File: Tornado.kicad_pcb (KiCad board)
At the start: 4 copper layers, 22.9 x 22.9 mm, 42 parts, among them J1 MOLEX, SW1 ID, U1 AP63205WU, U2 STM32G431KBUx, U3 LSM6DS3, U4 AP2112K-3.3, U5 TCAN1057A, Y1 32MHz

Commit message: Fixed silkscreen
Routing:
- net /ID_SW: track 16.1 -> 17.7 mm
- net /SDA: track 27.1 -> 26.5 mm

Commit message: Changed ESD diode
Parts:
- D2: value ~ -> TVS; footprint Tornado_Footprints:TVS-2020 -> Diode_SMD:D_SOD-323
- U3: value LSM6DS3 -> LSM6DSV
- moved D2 0.10 mm to (148.5, 106.6)
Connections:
- D2 pad 1: GND -> +12V
- D2 pad 2: +12V -> GND
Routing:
- net GND: track 87.8 -> 81.9 mm, vias 19 -> 20

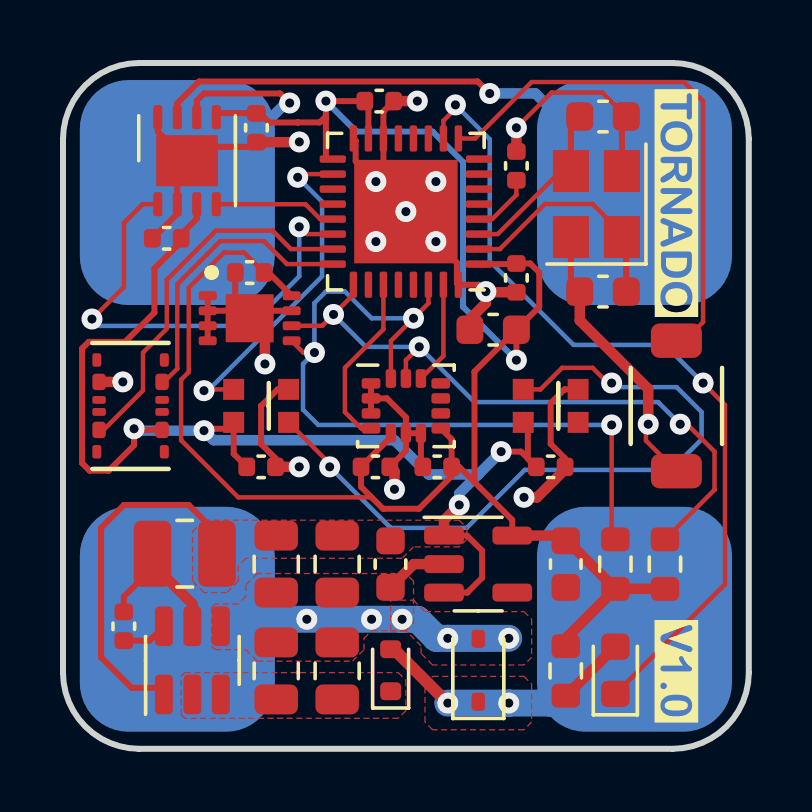
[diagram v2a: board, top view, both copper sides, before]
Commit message: Replaced pads with holes
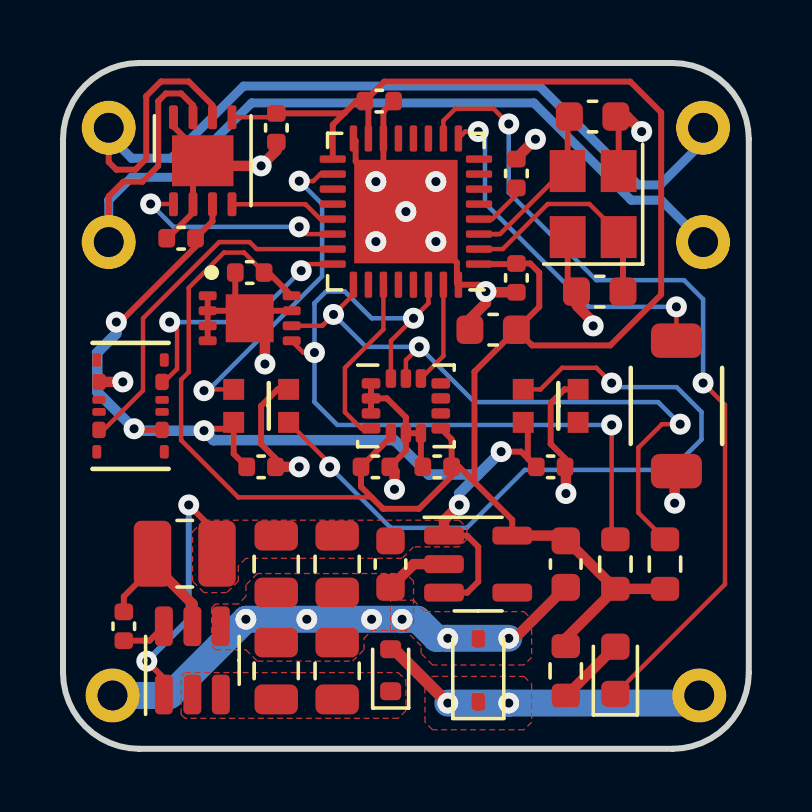
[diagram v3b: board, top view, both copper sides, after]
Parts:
- removed TP1: PWR, Tornado_Footprints:Wire_Pad
- removed TP2: GND, Tornado_Footprints:Wire_Pad
- removed TP3: CANH, Tornado_Footprints:Wire_Pad
- removed TP4: CANL, Tornado_Footprints:Wire_Pad
- added J2: PWR, Tornado_Footprints:Wire_Hole, F.Cu at (155.8, 107.4)
- added J3: CANH, Tornado_Footprints:Wire_Hole, F.Cu at (156.0, 92.3)
- added J3: CANH, Tornado_Footprints:Wire_Hole, F.Cu at (136.1, 92.3)
- added J4: CANL, Tornado_Footprints:Wire_Hole, F.Cu at (156.0, 88.5)
- added J4: CANL, Tornado_Footprints:Wire_Hole, F.Cu at (136.1, 88.5)
- added J5: GND, Tornado_Footprints:Wire_Hole, F.Cu at (136.3, 107.4)
- moved C10 0.66 mm to (141.7, 88.5)
- moved U5 0.52 mm to (139.3, 89.6)
- moved C9 0.48 mm to (138.6, 92.2)
- moved C15 0.35 mm to (152.3, 88.1)
- moved C20 0.25 mm to (149.7, 90.0)
- moved C16 0.11 mm to (152.5, 94.0)
- moved Y1 0.11 mm to (152.3, 91.1)
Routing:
- net /CANL: track 8.86 -> 31.7 mm, vias 1 -> 0
- net /CANH: track 17.5 -> 32.1 mm, vias 1 -> 0
- net /TX: track 15.6 -> 7.25 mm
- net +3.3V: track 68.7 -> 76.2 mm, vias 2 -> 0
- net +5V: track 52.3 -> 44.9 mm, vias 4 -> 7
- net /ID_SW: track 17.7 -> 12.4 mm, vias 0 -> 2
- net GND: track 81.9 -> 78.2 mm, vias 20 -> 22
- net +12V: track 10.0 -> 11.1 mm
- net /SWCLK: track 9.60 -> 8.58 mm, vias 0 -> 2
- net /SDA: track 26.5 -> 25.9 mm
- net /SWDIO: track 12.5 -> 11.9 mm
- net /RX: track 4.14 -> 3.56 mm

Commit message: Added Silkscreen
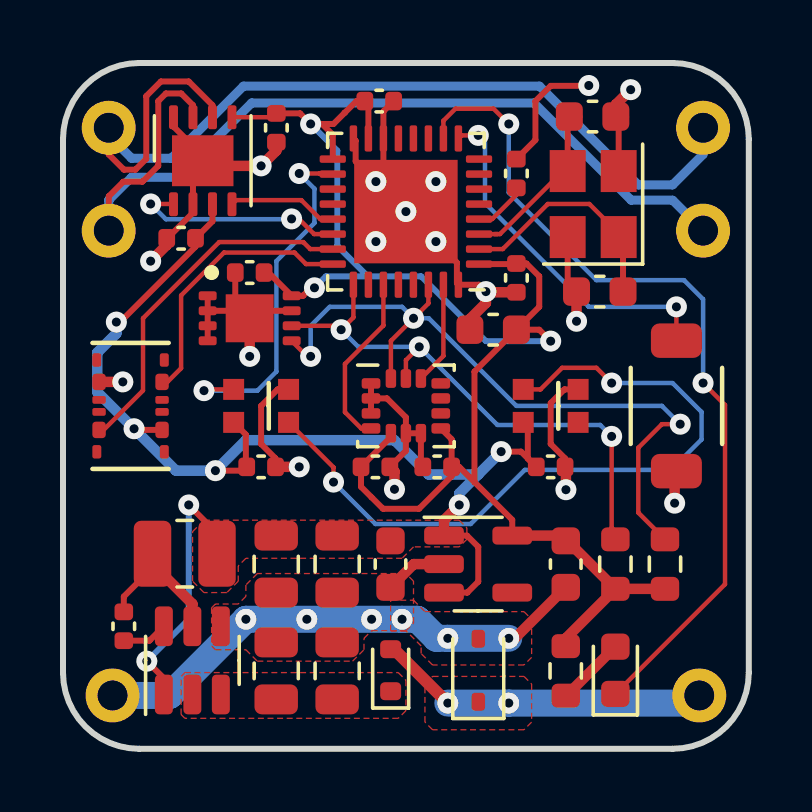
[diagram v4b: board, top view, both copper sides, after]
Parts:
- moved R1 1.65 mm to (153.0, 103.1)
- moved R2 1.65 mm to (154.7, 103.1)
- moved J3 0.38 mm to (156.0, 91.9)
- moved J3 0.38 mm to (136.1, 91.9)
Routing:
- net +3.3V: track 76.2 -> 55.4 mm, vias 0 -> 3
- net /SCL: track 22.4 -> 18.7 mm
- net GND: track 78.2 -> 81.5 mm, vias 22 -> 23
- net +5V: track 44.9 -> 46.0 mm
- net /RGB: track 11.2 -> 12.2 mm
- net /CANH: track 32.1 -> 31.1 mm
- net /SDA: track 25.9 -> 25.0 mm
- net /SWCLK: track 8.58 -> 9.06 mm, vias 2 -> 0

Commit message: Added Ferrite Bead
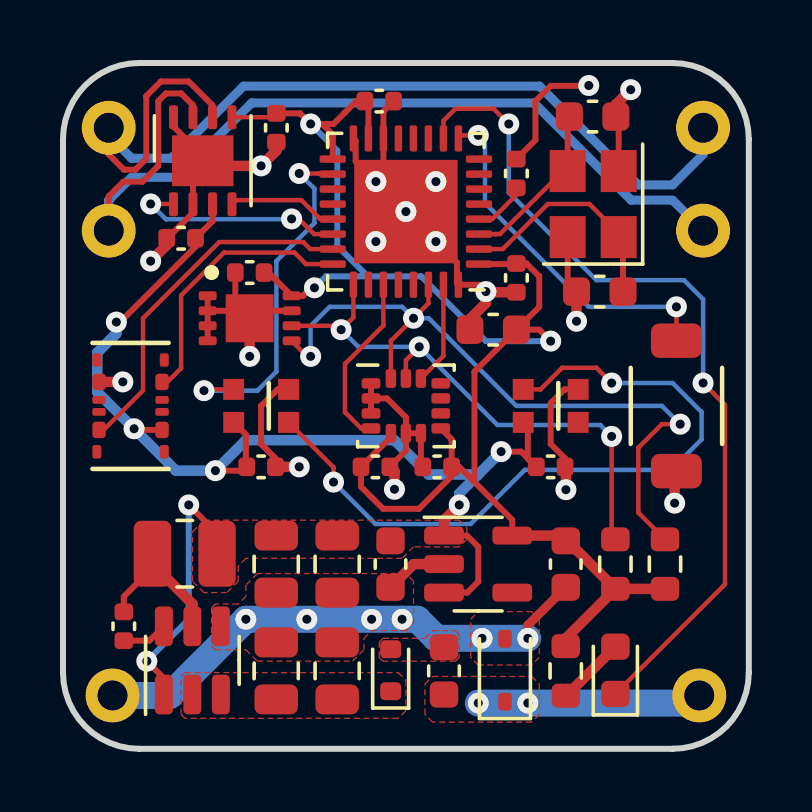
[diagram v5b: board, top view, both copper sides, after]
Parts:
- added FB1: FerriteBead, Inductor_SMD:L_0603_1608Metric, F.Cu at (147.3, 106.6)
- R1, R2, R3: value 4.7K -> 3k
- U6: value ~ -> M34E04
- moved D2 0.89 mm to (149.4, 106.6)
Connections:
- D1 pad 2: +12V -> Net-(D1-A)
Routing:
- net +12V: track 11.1 -> 7.47 mm
- added copper zone on F.Cu, net Net-(D1-A)

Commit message: Added resistor to filter
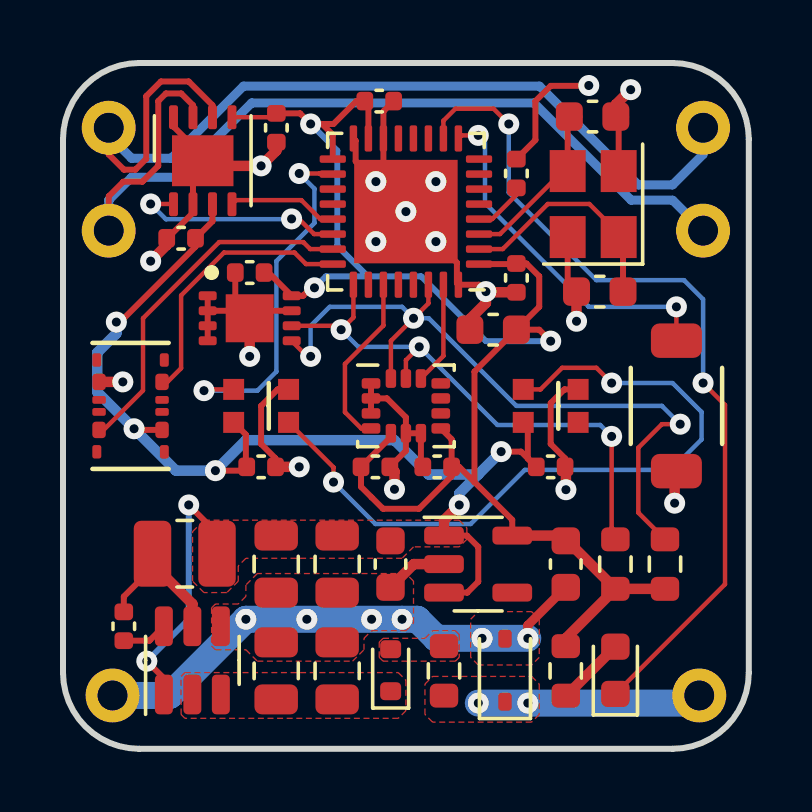
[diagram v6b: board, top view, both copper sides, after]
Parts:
- removed FB1: FerriteBead, Inductor_SMD:L_0603_1608Metric
- added R4: 5, Resistor_SMD:R_0603_1608Metric, F.Cu at (147.3, 106.6)
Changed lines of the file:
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@@
       (net 38 "+5V") (pinfunction "VDD") (pintype "power_in") (thermal_bridge_angle 45))
   )
-  (footprint "Inductor_SMD:L_0603_1608Metric" (layer "F.Cu")
-    (at 147.32 106.623 90)
-    (descr "Inductor SMD 0603 (1608 Metric), square (rectangular) end terminal, IPC_7351 nominal, (Body size source: http://www.tortai-tech.com/upload/download/2011102023233369053.pdf), generated with kicad-footprint-generator")
-    (tags "inductor")
-    (property "Sheetfile" "Tornado.kicad_sch")
-    (property "Sheetname" "")
-    (property "ki_description" "Ferrite bead")
-    (property "ki_keywords" "L ferrite bead inductor filter")
-    (attr smd)
-    (fp_text reference "FB1" (at 0 -1.43 90) (layer "F.SilkS") hide
-        (effects (font (size 1 1) (thickness 0.15)))
-    )
-    (fp_text value "FerriteBead" (at 0 1.43 90) (layer "F.Fab") hide
-        (effects (font (size 1 1) (thickness 0.15)))
-    )
-    (fp_text user "${REFERENCE}" (at 0 0 90) (layer "F.Fab")
-        (effects (font (size 0.4 0.4) (thickness 0.06)))
-    )
-    (fp_line (start -0.162779 -0.51) (end 0.162779 -0.51)
-      (stroke (width 0.12) (type solid)) (layer "F.SilkS"))
-    (fp_line (start -0.162779 0.51) (end 0.162779 0.51)
-      (stroke (width 0.12) (type solid)) (layer "F.SilkS"))
-    (fp_line (start -1.48 -0.73) (end 1.48 -0.73)
-      (stroke (width 0.05) (type solid)) (layer "F.CrtYd"))
-    (fp_line (start -1.48 0.73) (end -1.48 -0.73)
-      (stroke (width 0.05) (type solid)) (layer "F.CrtYd"))
-    (fp_line (start 1.48 -0.73) (end 1.48 0.73)
-      (stroke (width 0.05) (type solid)) (layer "F.CrtYd"))
-    (fp_line (start 1.48 0.73) (end -1.48 0.73)
-      (stroke (width 0.05) (type solid)) (layer "F.CrtYd"))
-    (fp_line (start -0.8 -0.4) (end 0.8 -0.4)
-      (stroke (width 0.1) (type solid)) (layer "F.Fab"))
-    (fp_line (start -0.8 0.4) (end -0.8 -0.4)
-      (stroke (width 0.1) (type solid)) (layer "F.Fab"))
-    (fp_line (start 0.8 -0.4) (end 0.8 0.4)
-      (stroke (width 0.1) (type solid)) (layer "F.Fab"))
-    (fp_line (start 0.8 0.4) (end -0.8 0.4)
-      (stroke (width 0.1) (type solid)) (layer "F.Fab"))
-    (pad "1" smd roundrect (at -0.7875 0 90) (size 0.875 0.95) (layers "F.Cu" "F.Paste" "F.Mask") (roundrect_rratio 0.25)
-      (net 41 "+12V") (pintype "passive"))
-    (pad "2" smd roundrect (at 0.7875 0 90) (size 0.875 0.95) (layers "F.Cu" "F.Paste" "F.Mask") (roundrect_rratio 0.25)
-      (net 47 "Net-(D1-A)") (pintype "passive"))
-    (model "${KICAD6_3DMODEL_DIR}/Inductor_SMD.3dshapes/L_0603_1608Metric.wrl"
-      (offset (xyz 0 0 0))
-      (scale (xyz 1 1 1))
-      (rotate (xyz 0 0 0))
-    )
-  )
   (footprint "Capacitor_SMD:C_0402_1005Metric" (layer "F.Cu")
     (at 149.733 90.043 90)
@@
         (effects (font (size 1 1) (thickness 0.15)))
     )
-    (fp_text user "${REFERENCE}" (at 0 -1.85 90) (layer "F.Fab")
-        (effects (font (size 1 1) (thickness 0.15)))
-    )
     (fp_line (start -1.61 -0.85) (end -1.61 0.85)
       (stroke (width 0.12) (type solid)) (layer "F.SilkS"))
@@
     )
   )
+  (footprint "Resistor_SMD:R_0603_1608Metric" (layer "F.Cu")
+    (at 147.32 106.623 -90)
+    (descr "Resistor SMD 0603 (1608 Metric), square (rectangular) end terminal, IPC_7351 nominal, (Body size source: IPC-SM-782 page 72, https://www.pcb-3d.com/wordpress/wp-content/uploads/ipc-sm-782a_amendment_1_and_2.pdf), generated with kicad-footprint-generator")
+    (tags "resistor")
+    (property "Sheetfile" "Tornado.kicad_sch")
+    (property "Sheetname" "")
+    (property "ki_description" "Resistor")
+    (property "ki_keywords" "R res resistor")
+    (attr smd)
+    (fp_text reference "R4" (at 0 -1.43 90) (layer "F.SilkS") hide
+        (effects (font (size 1 1) (thickness 0.15)))
+    )
+    (fp_text value "5" (at 0 1.43 90) (layer "F.Fab") hide
+        (effects (font (size 1 1) (thickness 0.15)))
+    )
+    (fp_text user "${REFERENCE}" (at 0 0 90) (layer "F.Fab")
+        (effects (font (size 0.4 0.4) (thickness 0.06)))
+    )
+    (fp_line (start -0.237258 -0.5225) (end 0.237258 -0.5225)
+      (stroke (width 0.12) (type solid)) (layer "F.SilkS"))
+    (fp_line (start -0.237258 0.5225) (end 0.237258 0.5225)
+      (stroke (width 0.12) (type solid)) (layer "F.SilkS"))
+    (fp_line (start -1.48 -0.73) (end 1.48 -0.73)
+      (stroke (width 0.05) (type solid)) (layer "F.CrtYd"))
+    (fp_line (start -1.48 0.73) (end -1.48 -0.73)
+      (stroke (width 0.05) (type solid)) (layer "F.CrtYd"))
+    (fp_line (start 1.48 -0.73) (end 1.48 0.73)
+      (stroke (width 0.05) (type solid)) (layer "F.CrtYd"))
+    (fp_line (start 1.48 0.73) (end -1.48 0.73)
+      (stroke (width 0.05) (type solid)) (layer "F.CrtYd"))
+    (fp_line (start -0.8 -0.4125) (end 0.8 -0.4125)
+      (stroke (width 0.1) (type solid)) (layer "F.Fab"))
+    (fp_line (start -0.8 0.4125) (end -0.8 -0.4125)
+      (stroke (width 0.1) (type solid)) (layer "F.Fab"))
+    (fp_line (start 0.8 -0.4125) (end 0.8 0.4125)
+      (stroke (width 0.1) (type solid)) (layer "F.Fab"))
+    (fp_line (start 0.8 0.4125) (end -0.8 0.4125)
+      (stroke (width 0.1) (type solid)) (layer "F.Fab"))
+    (pad "1" smd roundrect (at -0.825 0 270) (size 0.8 0.95) (layers "F.Cu" "F.Paste" "F.Mask") (roundrect_rratio 0.25)
+      (net 47 "Net-(D1-A)") (pintype "passive"))
+    (pad "2" smd roundrect (at 0.825 0 270) (size 0.8 0.95) (layers "F.Cu" "F.Paste" "F.Mask") (roundrect_rratio 0.25)
+      (net 41 "+12V") (pintype "passive"))
+    (model "${KICAD6_3DMODEL_DIR}/Resistor_SMD.3dshapes/R_0603_1608Metric.wrl"
+      (offset (xyz 0 0 0))
+      (scale (xyz 1 1 1))
+      (rotate (xyz 0 0 0))
+    )
+  )
   (gr_poly
     (pts
@@
   (segment (start 151.55 89.9625) (end 151.2105 89.9625) (width 0.15) (layer "F.Cu") (net 2))
   (segment (start 151.500526 89.6855) (end 151.55 89.6855) (width 0.15) (layer "F.Cu") (net 2))
-  (segment (start 149.11 92.063) (end 148.4875 92.063) (width 0.15) (layer "F.Cu") (net 2))
-  (segment (start 149.186526 92.063) (end 149.002375 92.063) (width 0.15) (layer "F.Cu") (net 2))
+  (segment (start 149.186526 92.063) (end 148.4875 92.063) (width 0.15) (layer "F.Cu") (net 2))
   (segment (start 151.102875 89.9625) (end 151.102875 90.146651) (width 0.15) (layer "F.Cu") (net 2))
   (segment (start 151.845 89.3905) (end 151.55 89.6855) (width 0.2) (layer "F.Cu") (net 2))
@@
   (segment (start 142.624 94.119) (end 142.243 94.119) (width 0.2) (layer "F.Cu") (net 40))
   (segment (start 150.495 94.488) (end 150.495 93.472) (width 0.2) (layer "F.Cu") (net 40))
-  (segment (start 144.018 88.011) (end 143.99 88.039) (width 0.2) (layer "F.Cu") (net 40))
   (segment (start 143.6125 88.7485) (end 143.6125 89.563) (width 0.2) (layer "F.Cu") (net 40))
+  (segment (start 143.637 88.392) (end 144.399 87.63) (width 0.2) (layer "F.Cu") (net 40))
   (segment (start 144.554 99.822) (end 145.55 98.826) (width 0.2) (layer "F.Cu") (net 40))
   (segment (start 149.595 102.113) (end 151.2035 102.113) (width 0.35) (layer "F.Cu") (net 40))
@@
   (segment (start 143.256 88.392) (end 143.6125 88.7485) (width 0.2) (layer "F.Cu") (net 40))
   (segment (start 148.336 100.33) (end 148.336 96.647) (width 0.2) (layer "F.Cu") (net 40))
+  (segment (start 144.399 87.63) (end 144.681 87.63) (width 0.2) (layer "F.Cu") (net 40))
   (segment (start 141.323 93.345) (end 141.469 93.345) (width 0.2) (layer "F.Cu") (net 40))
   (segment (start 140.419 88.168) (end 141.603 88.168) (width 0.15) (layer "F.Cu") (net 40))
@@
   (segment (start 150.495 93.472) (end 150.066 93.043) (width 0.2) (layer "F.Cu") (net 40))
   (segment (start 151.3785 105.798) (end 151.3785 105.54175) (width 0.35) (layer "F.Cu") (net 40))
-  (segment (start 144.018 88.011) (end 144.399 87.63) (width 0.2) (layer "F.Cu") (net 40))
   (segment (start 153.03225 103.888) (end 154.686 103.888) (width 0.35) (layer "F.Cu") (net 40))
   (segment (start 143.002 93.853) (end 142.89 93.853) (width 0.2) (layer "F.Cu") (net 40))
@@
   (segment (start 147.574 98.9015) (end 147.2125 98.54) (width 0.2) (layer "F.Cu") (net 40))
   (segment (start 142.522 88.039) (end 141.732 88.039) (width 0.2) (layer "F.Cu") (net 40))
-  (segment (start 144.399 87.63) (end 144.681 87.63) (width 0.2) (layer "F.Cu") (net 40))
   (segment (start 149.595 102.113) (end 149.595 101.589) (width 0.2) (layer "F.Cu") (net 40))
   (segment (start 144.681 87.63) (end 144.8 87.749) (width 0.2) (layer "F.Cu") (net 40))
@@
   (segment (start 144.907 100.838) (end 145.288 101.219) (width 0.2) (layer "F.Cu") (net 40))
   (segment (start 144.907 100.838) (end 144.554 100.485) (width 0.2) (layer "F.Cu") (net 40))
-  (segment (start 143.637 88.392) (end 144.018 88.011) (width 0.2) (layer "F.Cu") (net 40))
   (segment (start 141.469 93.345) (end 142.243 94.119) (width 0.2) (layer "F.Cu") (net 40))
   (segment (start 147.574 100.132) (end 147.574 99.822) (width 0.2) (layer "F.Cu") (net 40))
